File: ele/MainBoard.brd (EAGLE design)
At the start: 136.1 x 100 mm, 123 parts, among them IC1 MCP23017SP, IC2 74HC595D, IC3 74HC595D, X1 POWER_IN, X10 M7, X2 POWER_OUT, X3 M2, X4 M4, X5 M6, X6 M8, X7 M1, X8 M3, X9 M5

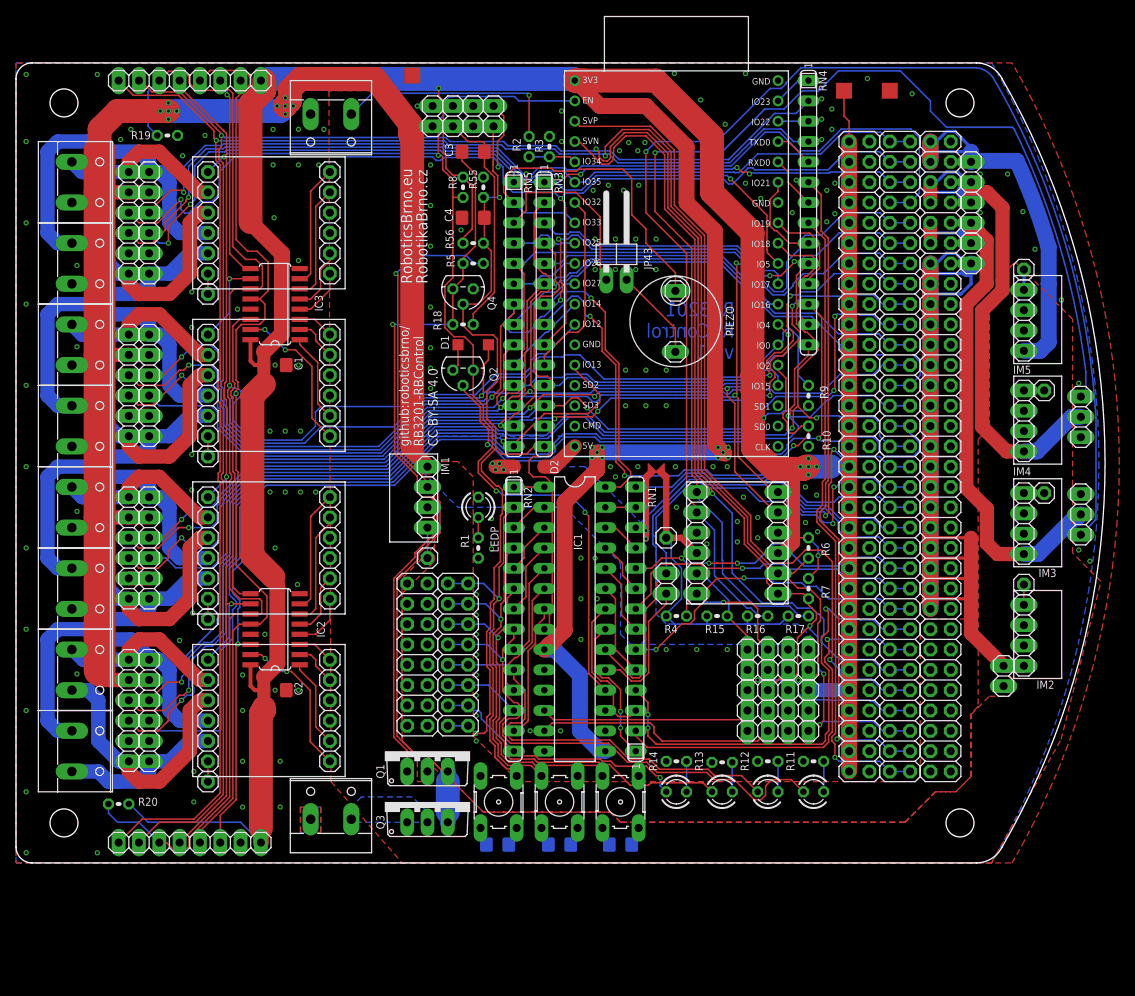
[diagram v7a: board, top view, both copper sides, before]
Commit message: ele: MainBoard - fix TO92 transistors pinout, change diodes package from SMD to TH, some signals routing improvements, fix some labels position, change version to 1.2
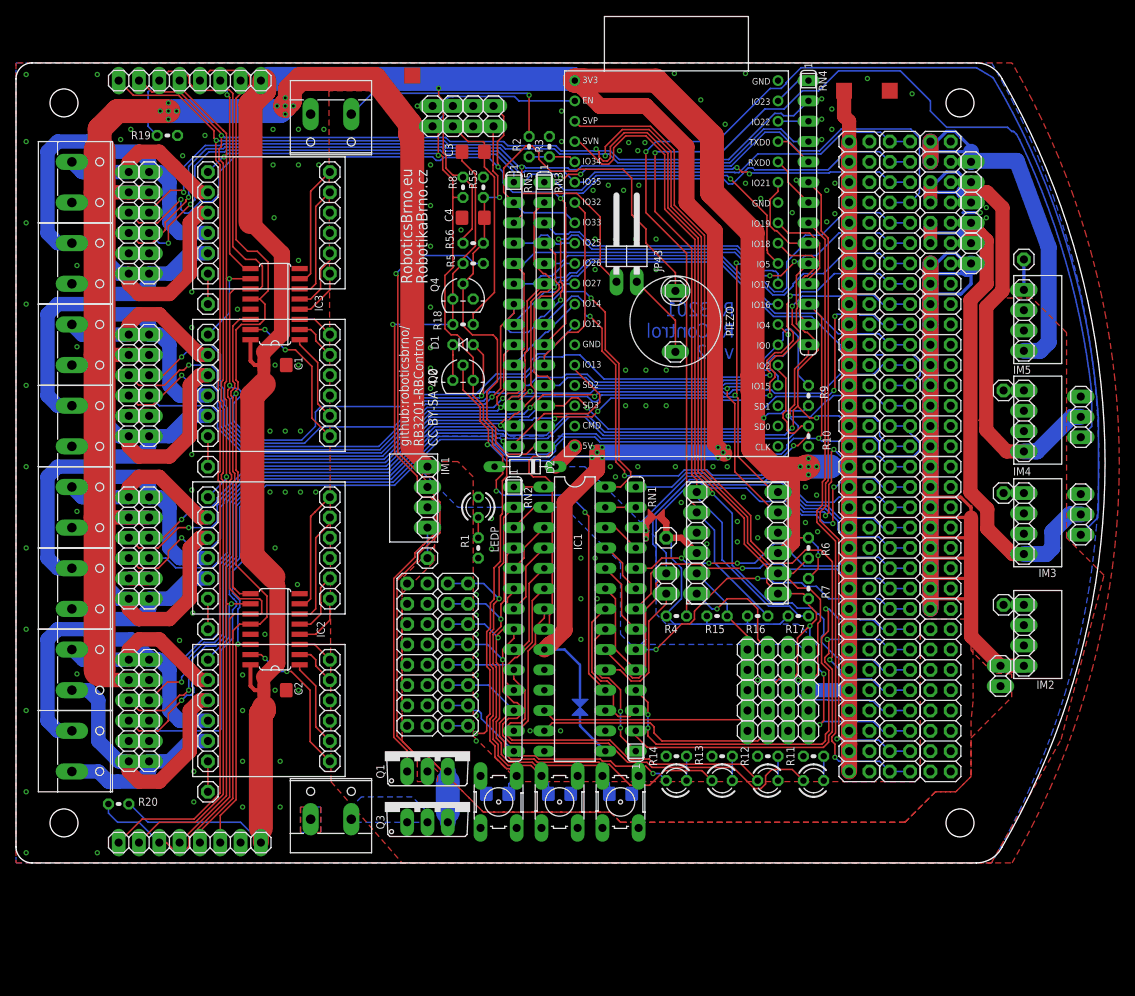
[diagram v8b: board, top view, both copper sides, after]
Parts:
- added U$1: SJ_NC, SolderJumperNormallyClosed:SJ_NC
- D1: device diode:SOD123 -> diode:D-2.5
- D2: device diode:SOD123 -> diode:D-7.5
- moved C5 6.35 mm to (60.2, 8.64)
- moved C6 6.35 mm to (67.9, 8.64)
- moved C7 6.35 mm to (75.6, 8.64)
- moved U$2 5.70 mm to (81.0, 44.2)
- moved JP3 5.08 mm to (123.4, 46.2)
- moved JP4 5.08 mm to (123.4, 59.1)
- moved JP2 3.59 mm to (123.4, 32.3)
- moved LED1 1.40 mm to (99.7, 10.3)
- moved LED2 1.40 mm to (94.0, 10.3)
- moved LED3 1.40 mm to (88.3, 10.3)
- moved LED4 1.40 mm to (82.5, 10.3)
- moved JP43 1.30 mm to (76.3, 76.5)
- moved JP30 1.27 mm to (24.0, 69.8)
- moved JP27 1.27 mm to (24.0, 8.89)
- moved JP28 1.27 mm to (24.0, 29.2)
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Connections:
- new net EXP_A0: IC1.15, U$1.P$2
- net +3V3: now also U$1.P$1; no longer IC1.15
- net EB0: no longer SW1.3
- net EB1: no longer SW2.4
- net EB2: no longer SW3.4
- net EN: now also Q2.3; no longer Q2.1
- net GND: now also Q4.3; no longer Q4.1
- net START_GATE: now also Q4.1; no longer Q4.3
- net _EN_: now also Q2.1; no longer Q2.3
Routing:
- net 5V_2: track 153.9 -> 168.6 mm
- net +5V: track 205.1 -> 196.7 mm, vias 16 -> 12
- net EXP_A0: track 0.00 -> 6.19 mm
- net HVIOREF: track 42.7 -> 37.0 mm
- net GND: track 14.9 -> 9.91 mm, vias 156 -> 147
- net B5V: track 157.0 -> 161.6 mm
- net ESP_!SHUTDOWN: track 103.2 -> 98.7 mm
- net +3V3: track 552.1 -> 547.6 mm
- net ENC7B_: track 45.8 -> 49.4 mm
- net ENC7A: track 145.0 -> 146.5 mm
- net +5V_ESP: track 4.87 -> 3.54 mm
- net !FAULT3: track 2.54 -> 3.81 mm
- net !FAULT1: track 2.54 -> 3.81 mm
- net !FAULT0: track 2.54 -> 3.81 mm
- net STEP5_EN: track 2.54 -> 3.81 mm
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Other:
- board text added: "RB3201 RBControl v1.2"
- board text added: "RB3201-RBControl v1.2"
- board text removed: "RB3201 RBControl v1.1"
- board text removed: "RB3201-RBControl v1.1"
